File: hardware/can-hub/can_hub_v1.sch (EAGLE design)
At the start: 7 parts, among them J1 PJ-30220, J2 PJ-30220, J3 PJ-30220, J4 PJ-30220, J5 PJ-30220, J6 PJ-30220

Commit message: chore: fill schematic title blocks with CBA credit and doc numbers
Co-Authored-By: Claude Opus 4.6 <noreply@anthropic.com>
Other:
- note added: "1.0"
- note added: "CAN Bus Academy (canbusacademy.com)"
- note added: "CBA-CAN-HUB-001"
- note added: "Design: Igor Ramos | License: Open Source Hardware"
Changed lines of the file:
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@@
 <sheet>
 <plain>
+<text x="187.96" y="11.43" size="2.54" layer="94" font="vector">CBA-CAN-HUB-001</text>
+<text x="244.475" y="11.43" size="2.54" layer="94" font="vector">1.0</text>
+<text x="148.59" y="30.48" size="2.54" layer="94" font="vector">CAN Bus Academy (canbusacademy.com)</text>
+<text x="148.59" y="25.4" size="1.778" layer="94" font="vector">Design: Igor Ramos | License: Open Source Hardware</text>
 </plain>
 <instances>

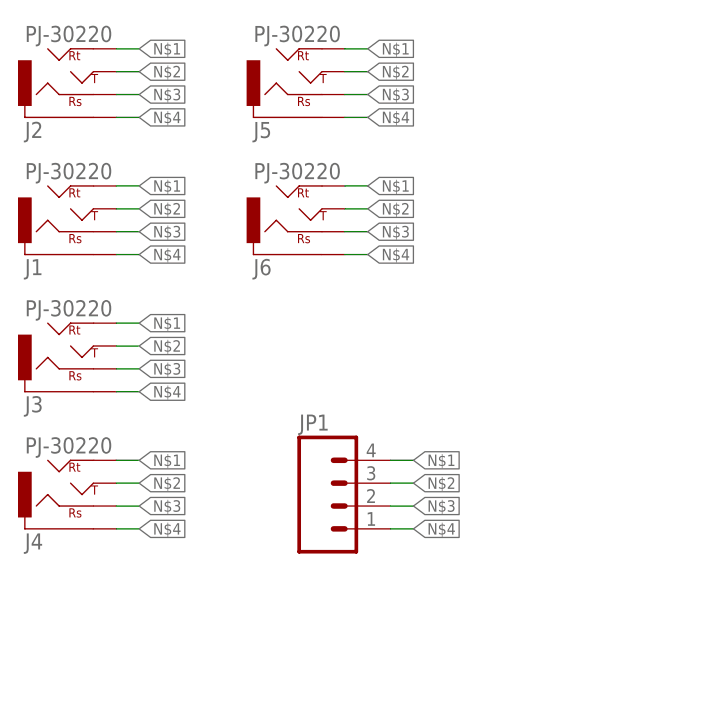
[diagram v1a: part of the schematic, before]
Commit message: fix: add net names to hub schematic, rename adapter files to db9_trs_adapter
- Hub: N$1→RING2, N$2→CAN_H, N$3→CAN_L, N$4→GND
- Adapter: adapter1.* → db9_trs_adapter.* (schematic, board, gerbers)

Co-Authored-By: Claude Opus 4.6 <noreply@anthropic.com>
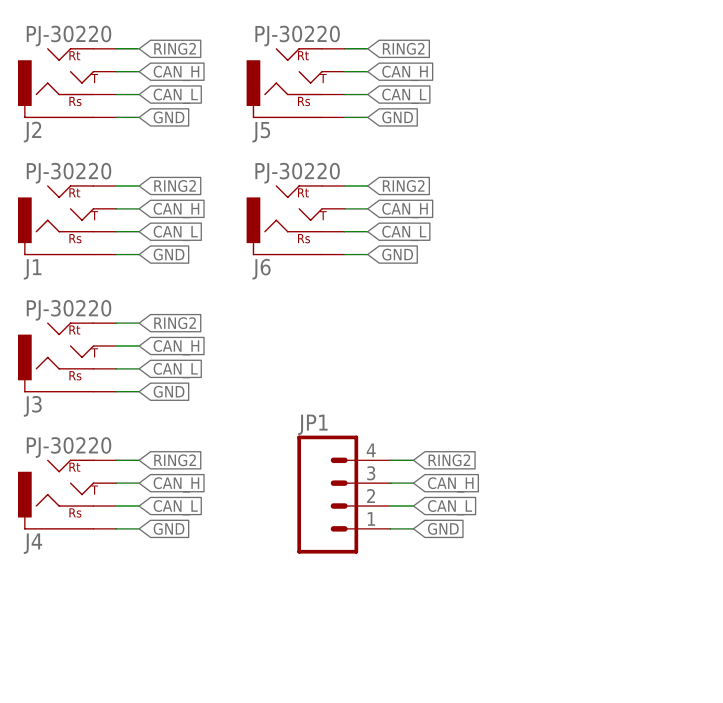
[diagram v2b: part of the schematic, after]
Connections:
- net N$1 renamed RING2
- net N$2 renamed CAN_H
- net N$3 renamed CAN_L
- net N$4 renamed GND
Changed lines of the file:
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@@
 </busses>
 <nets>
-<net name="N$1" class="0">
+<net name="RING2" class="0">
 <segment>
 <pinref part="J2" gate="G$1" pin="RT"/>
@@
 </segment>
 </net>
-<net name="N$2" class="0">
+<net name="CAN_H" class="0">
 <segment>
 <pinref part="J2" gate="G$1" pin="TIP"/>
@@
 </segment>
 </net>
-<net name="N$3" class="0">
+<net name="CAN_L" class="0">
 <segment>
 <pinref part="J2" gate="G$1" pin="RS"/>
@@
 </segment>
 </net>
-<net name="N$4" class="0">
+<net name="GND" class="0">
 <segment>
 <pinref part="J2" gate="G$1" pin="SLEEVE"/>

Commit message: fix: correct hub net names — CAN_L is RT (Ring Tip), not RS
Matches adapter schematic: RT=CAN_L, RS=RING2 (unused on TRS)

Co-Authored-By: Claude Opus 4.6 <noreply@anthropic.com>
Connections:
- net CAN_L: now also J1.RT, J2.RT, J3.RT, J4.RT, J5.RT, J6.RT, JP1.4; no longer J1.RS, J2.RS, J3.RS, J4.RS, J5.RS, J6.RS, JP1.2
- net RING2: now also J1.RS, J2.RS, J3.RS, J4.RS, J5.RS, J6.RS, JP1.2; no longer J1.RT, J2.RT, J3.RT, J4.RT, J5.RT, J6.RT, JP1.4
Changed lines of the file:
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@@
 </busses>
 <nets>
-<net name="RING2" class="0">
+<net name="CAN_L" class="0">
 <segment>
 <pinref part="J2" gate="G$1" pin="RT"/>
@@
 </segment>
 </net>
-<net name="CAN_L" class="0">
+<net name="RING2" class="0">
 <segment>
 <pinref part="J2" gate="G$1" pin="RS"/>
